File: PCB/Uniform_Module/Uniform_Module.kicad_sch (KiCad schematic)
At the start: 16 parts, among them J1 PCIE_x1_Conn_01x36_Male, SW1 Button_SMD_PTS_647_SN50_SMTR2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, SW2 Button_SMD_PTS_647_SN50_SMTR2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, U1 STM32L072KZT6

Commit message: began routing for uniform module
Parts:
- J1: footprint (none) -> Uniform:SAMTEC_PCIE_x1_CARD_EDGE_02_X_D_TH
- SW1, SW2: footprint PTS 647 SN50 SMTR2 LFS -> Uniform:Button SMD PTS 647 SN50 SMTR2 LFS
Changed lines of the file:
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@@
   (symbol (lib_id "power:+3.3V") (at 177.8 107.95 90) (unit 1)
     (in_bom yes) (on_board yes)
-    (property "Reference" "#PWR?" (id 0) (at 181.61 107.95 0)
+    (property "Reference" "#PWR0117" (id 0) (at 181.61 107.95 0)
       (effects (font (size 1.27 1.27)) hide)
     )
@@
   (symbol (lib_id "power:GND") (at 203.2 129.54 90) (unit 1)
     (in_bom yes) (on_board yes)
-    (property "Reference" "#PWR?" (id 0) (at 209.55 129.54 0)
+    (property "Reference" "#PWR0118" (id 0) (at 209.55 129.54 0)
       (effects (font (size 1.27 1.27)) hide)
     )
@@
   (symbol (lib_id "power:+5V") (at 160.02 165.1 270) (unit 1)
     (in_bom yes) (on_board yes)
-    (property "Reference" "#PWR?" (id 0) (at 156.21 165.1 0)
+    (property "Reference" "#PWR0112" (id 0) (at 156.21 165.1 0)
       (effects (font (size 1.27 1.27)) hide)
     )
@@
   (symbol (lib_id "power:GND") (at 223.52 107.95 90) (unit 1)
     (in_bom yes) (on_board yes)
-    (property "Reference" "#PWR?" (id 0) (at 229.87 107.95 0)
+    (property "Reference" "#PWR0113" (id 0) (at 229.87 107.95 0)
       (effects (font (size 1.27 1.27)) hide)
     )
@@
       (effects (font (size 1.524 1.524)))
     )
-    (property "Footprint" "PTS 647 SN50 SMTR2 LFS" (id 2) (at 190.5 109.22 0)
+    (property "Footprint" "Uniform:Button SMD PTS 647 SN50 SMTR2 LFS" (id 2) (at 190.5 109.22 0)
       (effects (font (size 1.27 1.27) italic) hide)
     )
@@
   (symbol (lib_id "power:+3.3V") (at 157.48 129.54 90) (unit 1)
     (in_bom yes) (on_board yes)
-    (property "Reference" "#PWR?" (id 0) (at 161.29 129.54 0)
+    (property "Reference" "#PWR0110" (id 0) (at 161.29 129.54 0)
       (effects (font (size 1.27 1.27)) hide)
     )
@@
   (symbol (lib_id "power:GND") (at 342.9 190.5 90) (unit 1)
     (in_bom yes) (on_board yes)
-    (property "Reference" "#PWR?" (id 0) (at 349.25 190.5 0)
+    (property "Reference" "#PWR0114" (id 0) (at 349.25 190.5 0)
       (effects (font (size 1.27 1.27)) hide)
     )
@@
   (symbol (lib_id "power:+5V") (at 337.82 147.32 270) (unit 1)
     (in_bom yes) (on_board yes)
-    (property "Reference" "#PWR?" (id 0) (at 334.01 147.32 0)
+    (property "Reference" "#PWR0115" (id 0) (at 334.01 147.32 0)
       (effects (font (size 1.27 1.27)) hide)
     )
@@
   (symbol (lib_id "power:GND") (at 342.9 144.78 90) (unit 1)
     (in_bom yes) (on_board yes)
-    (property "Reference" "#PWR?" (id 0) (at 349.25 144.78 0)
+    (property "Reference" "#PWR0116" (id 0) (at 349.25 144.78 0)
       (effects (font (size 1.27 1.27)) hide)
     )
@@
   (symbol (lib_id "power:GND") (at 137.16 165.1 270) (unit 1)
     (in_bom yes) (on_board yes)
-    (property "Reference" "#PWR?" (id 0) (at 130.81 165.1 0)
+    (property "Reference" "#PWR0111" (id 0) (at 130.81 165.1 0)
       (effects (font (size 1.27 1.27)) hide)
     )
@@
     (property "Reference" "J1" (id 0) (at 325.12 97.79 0))
     (property "Value" "PCIE_x1_Conn_01x36_Male" (id 1) (at 325.12 100.33 0))
-    (property "Footprint" "" (id 2) (at 325.12 147.32 0)
+    (property "Footprint" "Uniform:SAMTEC_PCIE_x1_CARD_EDGE_02_X_D_TH" (id 2) (at 325.12 147.32 0)
       (effects (font (size 1.27 1.27)) hide)
     )
@@
       (effects (font (size 1.524 1.524)))
     )
-    (property "Footprint" "PTS 647 SN50 SMTR2 LFS" (id 2) (at 190.5 130.81 0)
+    (property "Footprint" "Uniform:Button SMD PTS 647 SN50 SMTR2 LFS" (id 2) (at 190.5 130.81 0)
       (effects (font (size 1.27 1.27) italic) hide)
     )
@@
       (reference "#PWR0109") (unit 1) (value "GND") (footprint "")
     )
+    (path "/558f6cf7-5b27-4837-8211-25ff6508bef9"
+      (reference "#PWR0110") (unit 1) (value "+3.3V") (footprint "")
+    )
+    (path "/c5ca0baa-14a9-46a7-a550-a13199207c5b"
+      (reference "#PWR0111") (unit 1) (value "GND") (footprint "")
+    )
+    (path "/1a0b9346-f53d-4472-87c4-a67ed029345f"
+      (reference "#PWR0112") (unit 1) (value "+5V") (footprint "")
+    )
+    (path "/22806f7a-57aa-4bc5-8eaf-0cb7892fe0a8"
+      (reference "#PWR0113") (unit 1) (value "GND") (footprint "")
+    )
+    (path "/8cacba12-5aae-4ccf-b922-889d7af4cf8f"
+      (reference "#PWR0114") (unit 1) (value "GND") (footprint "")
+    )
+    (path "/9818f90a-9321-4af7-816e-1d38b52d497d"
+      (reference "#PWR0115") (unit 1) (value "+5V") (footprint "")
+    )
+    (path "/bb4b86f3-d31d-4026-8d80-89e6f63a3e77"
+      (reference "#PWR0116") (unit 1) (value "GND") (footprint "")
+    )
+    (path "/167d34f8-7b19-4cdf-8fc2-ce22f223008d"
+      (reference "#PWR0117") (unit 1) (value "+3.3V") (footprint "")
+    )
+    (path "/17cbdd21-7ae4-482e-8b30-b65cc702cb8d"
+      (reference "#PWR0118") (unit 1) (value "GND") (footprint "")
+    )
     (path "/00000000-0000-0000-0000-000062453169"
       (reference "#PWR0120") (unit 1) (value "+3.3V") (footprint "")
@@
       (reference "#PWR0124") (unit 1) (value "+3.3V") (footprint "")
     )
-    (path "/167d34f8-7b19-4cdf-8fc2-ce22f223008d"
-      (reference "#PWR?") (unit 1) (value "+3.3V") (footprint "")
-    )
-    (path "/17cbdd21-7ae4-482e-8b30-b65cc702cb8d"
-      (reference "#PWR?") (unit 1) (value "GND") (footprint "")
-    )
-    (path "/1a0b9346-f53d-4472-87c4-a67ed029345f"
-      (reference "#PWR?") (unit 1) (value "+5V") (footprint "")
-    )
-    (path "/22806f7a-57aa-4bc5-8eaf-0cb7892fe0a8"
-      (reference "#PWR?") (unit 1) (value "GND") (footprint "")
-    )
-    (path "/558f6cf7-5b27-4837-8211-25ff6508bef9"
-      (reference "#PWR?") (unit 1) (value "+3.3V") (footprint "")
-    )
-    (path "/8cacba12-5aae-4ccf-b922-889d7af4cf8f"
-      (reference "#PWR?") (unit 1) (value "GND") (footprint "")
-    )
-    (path "/9818f90a-9321-4af7-816e-1d38b52d497d"
-      (reference "#PWR?") (unit 1) (value "+5V") (footprint "")
-    )
-    (path "/bb4b86f3-d31d-4026-8d80-89e6f63a3e77"
-      (reference "#PWR?") (unit 1) (value "GND") (footprint "")
-    )
-    (path "/c5ca0baa-14a9-46a7-a550-a13199207c5b"
-      (reference "#PWR?") (unit 1) (value "GND") (footprint "")
-    )
     (path "/00000000-0000-0000-0000-00006342748d"
       (reference "C1") (unit 1) (value "10uf") (footprint "Capacitor_SMD:C_0603_1608Metric_Pad1.08x0.95mm_HandSolder")
@@
     )
     (path "/cebbdf72-49e2-4e8c-8b32-f9cfe1d79f50"
-      (reference "J1") (unit 1) (value "PCIE_x1_Conn_01x36_Male") (footprint "")
+      (reference "J1") (unit 1) (value "PCIE_x1_Conn_01x36_Male") (footprint "Uniform:SAMTEC_PCIE_x1_CARD_EDGE_02_X_D_TH")
     )
     (path "/aefaa4bc-9b3d-4fb6-aee2-8b4a60a911ec"
@@
     )
     (path "/3396b43a-5a1d-49b8-a946-6fe71f36d85d"
-      (reference "SW1") (unit 1) (value "Button_SMD_PTS_647_SN50_SMTR2_LFS") (footprint "PTS 647 SN50 SMTR2 LFS")
+      (reference "SW1") (unit 1) (value "Button_SMD_PTS_647_SN50_SMTR2_LFS") (footprint "Uniform:Button SMD PTS 647 SN50 SMTR2 LFS")
     )
     (path "/daab072c-9433-43a5-9828-b5b77645268f"
-      (reference "SW2") (unit 1) (value "Button_SMD_PTS_647_SN50_SMTR2_LFS") (footprint "PTS 647 SN50 SMTR2 LFS")
+      (reference "SW2") (unit 1) (value "Button_SMD_PTS_647_SN50_SMTR2_LFS") (footprint "Uniform:Button SMD PTS 647 SN50 SMTR2 LFS")
     )
     (path "/00000000-0000-0000-0000-000062ef1199"

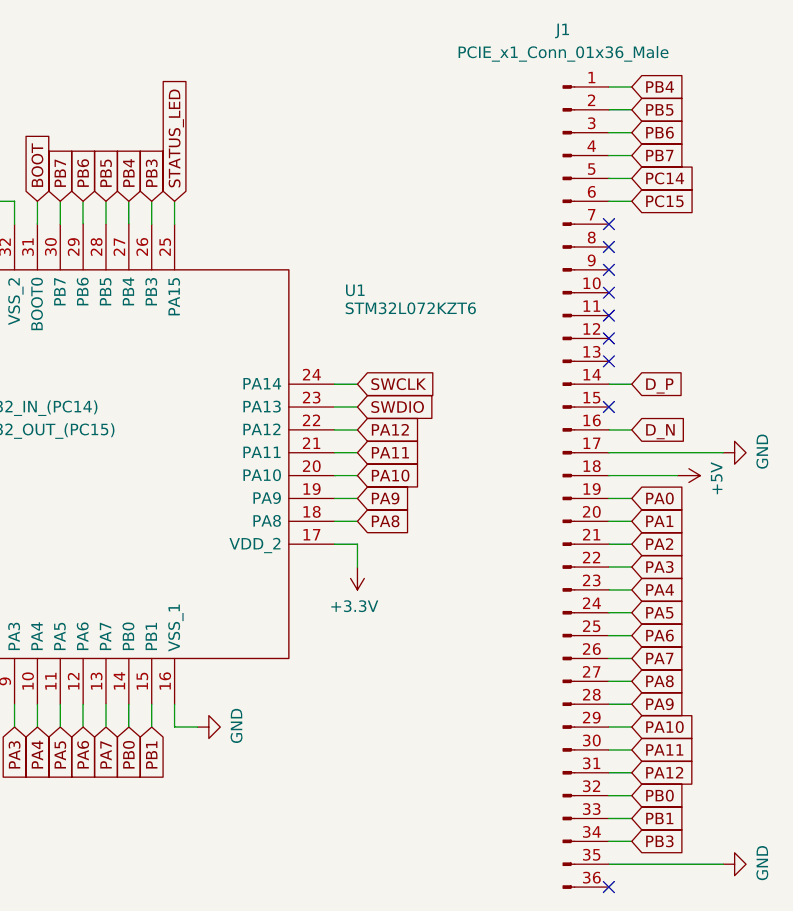
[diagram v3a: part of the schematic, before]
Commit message: clear all routing on module. Fix incorrect PCIE edge connector schematic net assignments
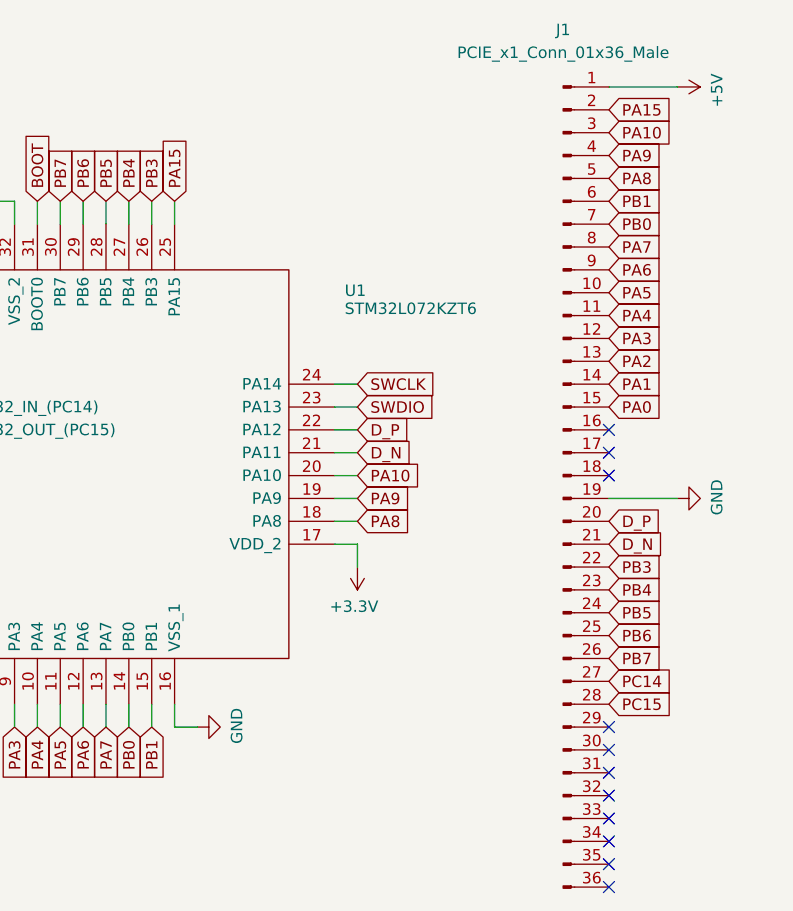
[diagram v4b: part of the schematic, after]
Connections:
- net +5V: now also J1.1 (Pin_1); no longer J1.18 (Pin_18)
- net D_N: now also J1.21 (Pin_21), U1.21 (PA11); no longer J1.16 (Pin_16)
- net D_P: now also J1.20 (Pin_20), U1.22 (PA12); no longer J1.14 (Pin_14)
- net GND: now also J1.19 (Pin_19); no longer J1.17 (Pin_17), J1.35 (Pin_35)
- net PA0: now also J1.15 (Pin_15); no longer J1.19 (Pin_19)
- net PA1: now also J1.14 (Pin_14); no longer J1.20 (Pin_20)
- net PA10: now also J1.3 (Pin_3); no longer J1.29 (Pin_29)
- net PA2: now also J1.13 (Pin_13); no longer J1.21 (Pin_21)
- net PA3: now also J1.12 (Pin_12); no longer J1.22 (Pin_22)
- net PA4: now also J1.11 (Pin_11); no longer J1.23 (Pin_23)
- net PA5: now also J1.10 (Pin_10); no longer J1.24 (Pin_24)
- net PA6: now also J1.9 (Pin_9); no longer J1.25 (Pin_25)
- net PA7: now also J1.8 (Pin_8); no longer J1.26 (Pin_26)
- net PA8: now also J1.5 (Pin_5); no longer J1.27 (Pin_27)
- net PA9: now also J1.4 (Pin_4); no longer J1.28 (Pin_28)
- net PB0: now also J1.7 (Pin_7); no longer J1.32 (Pin_32)
- net PB1: now also J1.6 (Pin_6); no longer J1.33 (Pin_33)
- net PB3: now also J1.22 (Pin_22); no longer J1.34 (Pin_34)
- net PB4: now also J1.23 (Pin_23); no longer J1.1 (Pin_1)
- net PB5: now also J1.24 (Pin_24); no longer J1.2 (Pin_2)
- net PB6: now also J1.25 (Pin_25); no longer J1.3 (Pin_3)
- net PB7: now also J1.26 (Pin_26); no longer J1.4 (Pin_4)
- net PC14: now also J1.27 (Pin_27); no longer J1.5 (Pin_5)
- net PC15: now also J1.28 (Pin_28); no longer J1.6 (Pin_6)
- net PA11: no longer names the net of J1.30 (Pin_30)
- net PA11: no longer U1.21 (PA11)
- net PA12: no longer names the net of J1.31 (Pin_31)
- net PA12: no longer U1.22 (PA12)
- net STATUS_LED renamed PA15
- net PA15: now also J1.2 (Pin_2)
- no-connect marks 13 -> 15

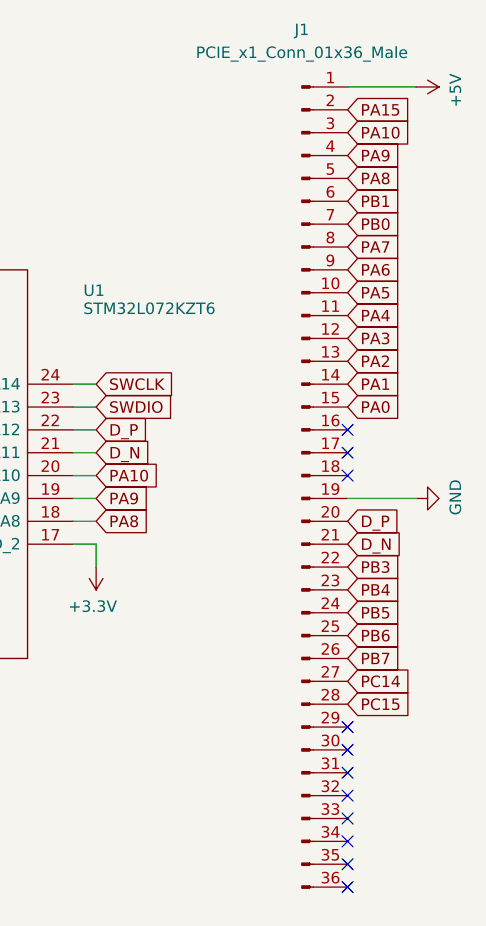
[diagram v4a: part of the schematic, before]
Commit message: improved trace origins on PCIE port/edge. Board rerouting done. Module rerouting in progress
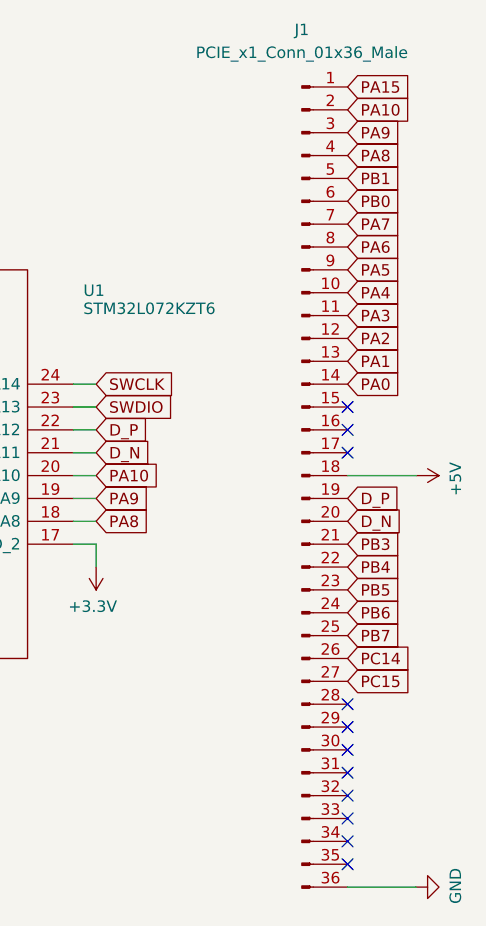
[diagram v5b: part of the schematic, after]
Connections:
- net +5V: now also J1.18 (Pin_18); no longer J1.1 (Pin_1)
- net D_N: now also J1.20 (Pin_20); no longer J1.21 (Pin_21)
- net D_P: now also J1.19 (Pin_19); no longer J1.20 (Pin_20)
- net GND: now also J1.36 (Pin_36); no longer J1.19 (Pin_19)
- net PA0: now also J1.14 (Pin_14); no longer J1.15 (Pin_15)
- net PA1: now also J1.13 (Pin_13); no longer J1.14 (Pin_14)
- net PA10: now also J1.2 (Pin_2); no longer J1.3 (Pin_3)
- net PA15: now also J1.1 (Pin_1); no longer J1.2 (Pin_2)
- net PA2: now also J1.12 (Pin_12); no longer J1.13 (Pin_13)
- net PA3: now also J1.11 (Pin_11); no longer J1.12 (Pin_12)
- net PA4: now also J1.10 (Pin_10); no longer J1.11 (Pin_11)
- net PA5: now also J1.9 (Pin_9); no longer J1.10 (Pin_10)
- net PA6: now also J1.8 (Pin_8); no longer J1.9 (Pin_9)
- net PA7: now also J1.7 (Pin_7); no longer J1.8 (Pin_8)
- net PA8: now also J1.4 (Pin_4); no longer J1.5 (Pin_5)
- net PA9: now also J1.3 (Pin_3); no longer J1.4 (Pin_4)
- net PB0: now also J1.6 (Pin_6); no longer J1.7 (Pin_7)
- net PB1: now also J1.5 (Pin_5); no longer J1.6 (Pin_6)
- net PB3: now also J1.21 (Pin_21); no longer J1.22 (Pin_22)
- net PB4: now also J1.22 (Pin_22); no longer J1.23 (Pin_23)
- net PB5: now also J1.23 (Pin_23); no longer J1.24 (Pin_24)
- net PB6: now also J1.24 (Pin_24); no longer J1.25 (Pin_25)
- net PB7: now also J1.25 (Pin_25); no longer J1.26 (Pin_26)
- net PC14: now also J1.26 (Pin_26); no longer J1.27 (Pin_27)
- net PC15: now also J1.27 (Pin_27); no longer J1.28 (Pin_28)
